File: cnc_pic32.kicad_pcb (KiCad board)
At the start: 4 copper layers, 96 x 96 mm, 121 parts, among them J1 icd, J10 tp_ft232_, J11 tp_ft232_, J12 tp_ft232_, J13 tp_ft232_, J14 tp_ft232_, J15 pololu, J16 pololu, J17 pololu, J18 pololu, J19 pololu, J2 USB_B_Mini, J20 pololu, J21 conector oled ST1306 128x32, J22 Adafruit ST7789, J23 mrf24j40_tp, J24 mrf24j40_tp, J3 tp_ft232_, J4 tp_ft232_, J5 USB_B_Mini, J6 tp_ft232_, J7 tp_ft232_, J8 tp_ft232_, J9 tp_ft232_, Q1 2N7002, SW1 power, SW2 up, SW3 down, SW4 left, SW5 rigth, U1 PIC32MX795F512L-80x-PF, U2 LM1117DT-3.3, U3 FT232BM, U4 LM1117DT-3.3, U5 MRF24J40MA, Y1 8MHZ, Y2 6MHZ

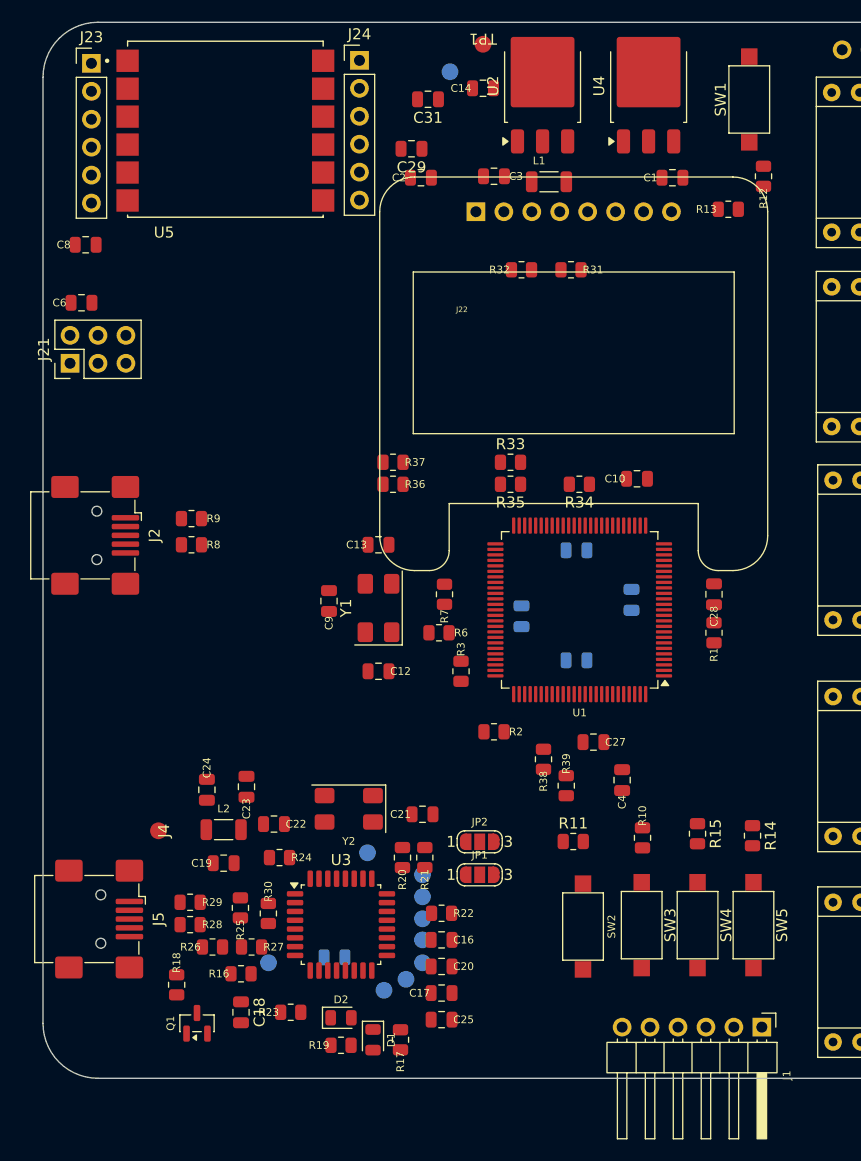
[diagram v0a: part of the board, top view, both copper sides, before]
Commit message: feat: 2-layer stackup, bus net class and schematic cleanup
PCB / project
- Reduce board from 4 layers to 2 (F.Cu / B.Cu) for cheaper fabrication
- Add "bus" net class and reorder net class priorities (bus 0, usb_differential 1, ...)

Schematics
- usb_conector_Ft232: add D+ / D-- labels on the USB mini-B data pair
- ft232: add 10K pull-ups, 100nf decoupling and test points on +3.3VA
- tp_ft232: remove solder jumpers JP1/JP2 (TX_Rpi / RX_Rpi now direct)
- Usb_pic32: add C38 100nf decoupling on +5V
- oled: expand connector J25 from 7 to 8 pins
- mcu / idc / power / zigbee / buttons / cnc_pic32: annotation and net cleanup

docs
- Add USB-Mini-B pinout reference images
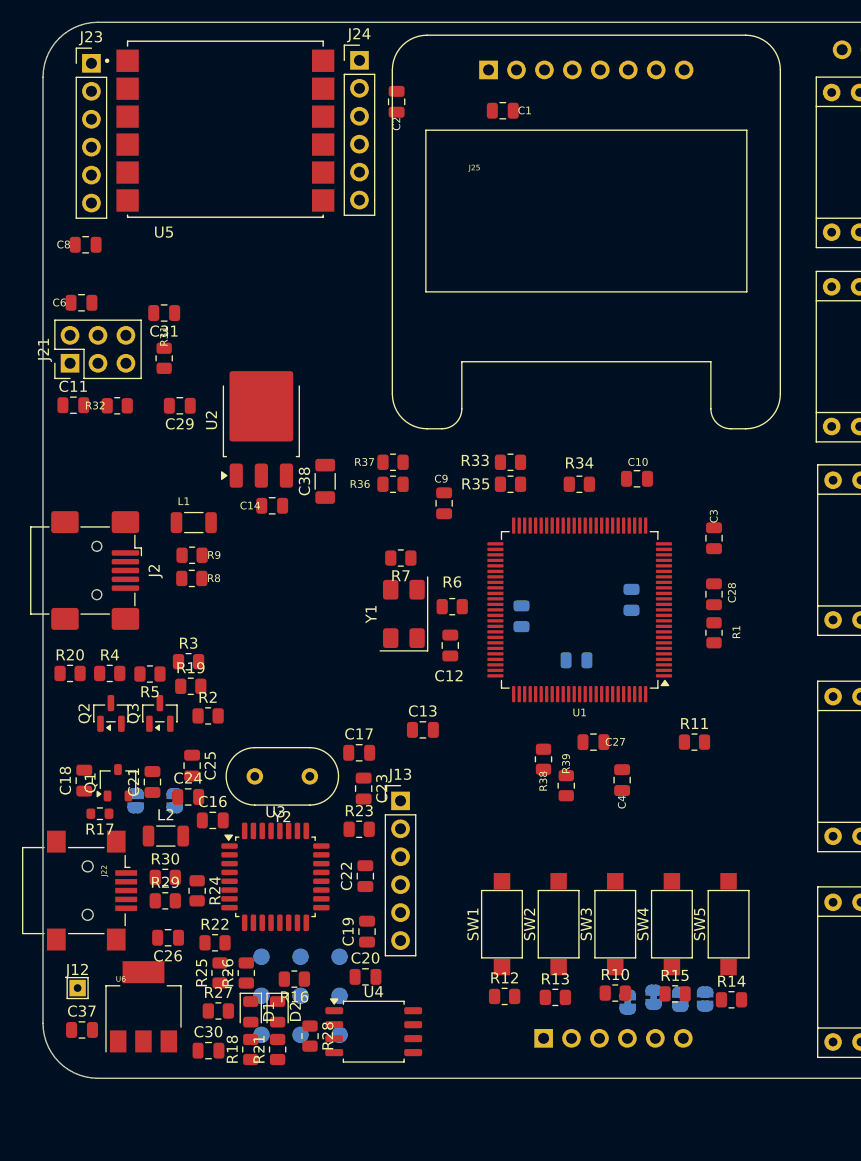
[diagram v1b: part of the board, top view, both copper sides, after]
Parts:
- removed J14: tp_ft232_, Library:connector_pin1
- removed TP1: tp_pic+5, Library:connector_pin1
- added C30: 100nf, Capacitor_SMD:C_0805_2012Metric, F.Cu at (67.0, 119.5)
- added C37: 100nf, Capacitor_SMD:C_0805_2012Metric, F.Cu at (55.5, 117.6)
- added C38: 100nf, Capacitor_SMD:C_1206_3216Metric, F.Cu at (77.7, 67.7)
- added J25: Conn_01x08_Pin, Library:Adafruit_SSD1306_No_Mounting_Holes_pads, F.Cu at (92.5, 30.3)
- added JP5: pgc1, Jumper:SolderJumper-2_P1.3mm_Open_RoundedPad1.0x1.5mm, B.Cu at (109.9, 114.8)
- added JP6: pgd1, Jumper:SolderJumper-2_P1.3mm_Open_RoundedPad1.0x1.5mm, B.Cu at (112.2, 114.8)
- added JP7: pgc2, Jumper:SolderJumper-2_P1.3mm_Bridged_RoundedPad1.0x1.5mm, B.Cu at (107.5, 114.6)
- added JP8: pgd2, Jumper:SolderJumper-2_P1.3mm_Bridged_RoundedPad1.0x1.5mm, B.Cu at (105.2, 115.1)
- added Q2: 2N7002, Package_TO_SOT_SMD:SOT-23, F.Cu at (58.2, 88.8)
- added Q3: 2N7002, Package_TO_SOT_SMD:SOT-23, F.Cu at (62.6, 88.8)
- added R4: 2k2, Resistor_SMD:R_0805_2012Metric, F.Cu at (58.1, 85.2)
- added R5: 2k2, Resistor_SMD:R_0805_2012Metric, F.Cu at (61.7, 85.2)
- added U6: LM1117DT-3.3, kiC:SOT-223-3_TabPin2, F.Cu at (61.1, 115.5)
- C11: moved to F.Cu
- C17, C18: value 33nf -> 100nf
- C21, C22: value 15p -> 100nf
- C23, C25: value 100nf -> 15p
- C24: value 100nf -> 33nf
- C26: value 100nf -> 33nf; moved to F.Cu
- J1: moved to B.Cu
- J10, J11, J3, J6, J7, J8, J9: value tp_ft232_ -> tp; footprint Library:connector_pin1 -> TestPoint:TestPoint_Pad_D1.5mm
- J12: value tp_ft232_ -> tp; footprint Library:connector_pin1 -> TestPoint:TestPoint_THTPad_1.5x1.5mm_Drill0.7mm; moved to F.Cu
- J13: value tp_ft232_ -> FT232RL; footprint Library:connector_pin1 -> Connector_PinHeader_2.54mm:PinHeader_1x06_P2.54mm_Vertical; moved to F.Cu
- J22: value Adafruit ST7789 -> USB_B_Mini; footprint Library:Adafruit_SSD1306_No_Mounting_Holes_pads -> kiC:USB_Mini-B_Lumberg_2486_01_Horizontal
- J4: value tp_ft232_ -> tp; footprint Library:connector_pin1 -> TestPoint:TestPoint_Pad_D1.5mm; moved to B.Cu
- J5: value USB_B_Mini -> tp; footprint Library:USB_Mini-B_Wuerth_65100516121_Horizontal -> TestPoint:TestPoint_Pad_D1.5mm; moved to B.Cu
- JP1, JP2: value SolderJumper_3_Bridged123 -> Jumper_Open; footprint Jumper:SolderJumper-3_P1.3mm_Open_RoundedPad1.0x1.5mm_NumberLabels -> Jumper:SolderJumper-2_P1.3mm_Open_RoundedPad1.0x1.5mm; moved to B.Cu
- Q1: value 2N7002 -> FDN306P; footprint Package_TO_SOT_SMD:SOT-23 -> Package_TO_SOT_SMD:SOT-23W
- R17: footprint Resistor_SMD:R_0805_2012Metric -> Resistor_SMD:R_0603_1608Metric
- R19: value 10K -> 100
- R2, R3: value 0 -> 2k2
- R21: value 100 -> 10K
- R23: value 10K -> 1K5
- R25: value 1K5 -> 10K
- R28: value 27 -> 2k2
- R30: value 10K -> 27
- U4: value LM1117DT-3.3 -> 93CxxA; footprint Package_TO_SOT_SMD:TO-252-3_TabPin2 -> Package_SO:SOIC-8_5.3x5.3mm_P1.27mm
- Y2: value 6MHZ -> Crystal; footprint Crystal:Crystal_SMD_0603-4Pin_6.0x3.5mm -> Crystal:Resonator-2Pin_W10.0mm_H5.0mm
- moved U4 89.5 mm to (82.1, 117.8), turned to 0 degrees
- moved SW1 78.3 mm to (93.7, 108.0)
- moved R12 78.2 mm to (94.0, 114.6), turned to 0 degrees
- moved R13 73.4 mm to (98.6, 114.6)
- moved J22 71.1 mm to (56.1, 104.9), turned to -90 degrees
- moved C11 47.6 mm to (54.8, 60.8)
- moved L1 44.7 mm to (65.7, 71.5)
- moved C14 42.5 mm to (72.8, 70.0)
- moved U2 39.7 mm to (71.9, 62.2)
- moved R32 38.8 mm to (58.7, 60.9)
- moved C3 38.5 mm to (113.0, 72.9), turned to -90 degrees
- moved R31 37.8 mm to (63.0, 56.5), turned to -90 degrees
- moved R19 35.4 mm to (65.4, 86.4)
- moved R20 34.5 mm to (54.5, 85.2), turned to 0 degrees
- moved R17 34.2 mm to (57.2, 97.9), turned to 180 degrees
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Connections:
- net /MCU/D+ renamed /D+
- net /MCU/D- renamed /D-
- net /MCU/RB0 renamed /MCU/PGC1
- net /MCU/RB1 renamed /MCU/PGD1
- net /MCU/RD4 renamed /RD4
- net /MCU/RD5 renamed /RD5
- net /MCU/RD6 renamed /RD6
- net /MCU/RF0 renamed /zigbee/MOSI_mrf
- net /MCU/RF1 renamed /zigbee/SCK_mrf
- net /MCU/RF12 renamed /zigbee/INT_mrf
- net /MCU/RF2 renamed /zigbee/MISO_mrf
- net /MCU/RF3 renamed /zigbee/CS_mrf
- net /MCU/RF4 renamed /zigbee/reset_mrf
- net /MCU/RF5 renamed /zigbee/wake_mrf
- net Net-(J2-D+) renamed /Usb_pic32/USB_D+
- net Net-(J2-D-) renamed /Usb_pic32/USB_D-
- A3 pad 16: /MCU/RB4 -> /MCU/PGM
- C14 pad 2: Net-(TP1-Pin_1) -> +5V
- C16 pad 1: /Ft232/mclr -> +3.3VA
- C16 pad 2: /Ft232/FT_CTS -> GND1
- C17 pad 1: Net-(U3-AVCC) -> +3.3VA
- C17 pad 2: GND -> GND1
- C18 pad 1: Net-(J3-Pin_1) -> Net-(C18-Pad1)
- C18 pad 2: GND -> +5VA
- C19 pad 1: GND -> GND1
- C19 pad 2: /Ft232/V+_USB -> +3.3VA
- C20 pad 1: GND -> GND1
- C20 pad 2: +3V3 -> +3.3VA
- C21 pad 1: /Ft232/FT_XTIN -> GND
- C21 pad 2: GND -> +5VA
- C22 pad 1: /Ft232/FT_XTOUT -> /Ft232/MCLR
- C22 pad 2: GND -> /Ft232/FT_CTS
- C23 pad 1: +3V3 -> /Ft232/FT_XTIN
- C24 pad 1: +3V3 -> Net-(U3-AVCC)
- C24 pad 2: GND -> GND1
- C25 pad 1: GND -> /Ft232/FT_XTOUT
- C25 pad 2: +3V3 -> GND
- C26 pad 1: GND -> Net-(J14-Pin_1)
- C26 pad 2: +3V3 -> GND1
- J1 pad 1: /Ft232/mclr -> /Ft232/MCLR
- J1 pad 4: /MCU/RC2 -> /Ft232/TX
- J1 pad 5: /MCU/RC3 -> /Ft232/RX
- J1 pad 6: /MCU/RC1 -> /MCU/PGM
- J12 pad 1: /Ft232/FT_RESET -> /Ft232/PWR
- J21 pad 1: GND -> +3.3V
- J21 pad 2: +3.3V -> +5V
- J21 pad 3: /MCU/sda -> /Oled/SDA
- J21 pad 4: /Oled/RG7 -> +5V
- J21 pad 5: /MCU/scl -> /Oled/SCL
- J21 pad 6: /Oled/RG8 -> GND
- J22 pad 1: GND -> Net-(J22-VBUS)
- J22 pad 2: +3.3V -> Net-(J22-D-)
- J22 pad 3: /MCU/sda -> Net-(J22-D+)
- J22 pad 4: /MCU/scl -> /Ft232/ID
- J22 pad 5: /Oled/RG0 -> GND
- J22 pad 6: /Oled/RG1 -> GND
- J3 pad 1: Net-(J3-Pin_1) -> /Ft232/FT_RST
- J4 pad 1: Net-(J4-Pin_1) -> /Ft232/FT_CTS
- J5 pad 1: Net-(J4-Pin_1) -> /Ft232/FT_DTR
- J6 pad 1: /Ft232/V+_USB -> /Ft232/FT_DRS
- J7 pad 1: /Ft232/FT_RI -> /Ft232/FT_DCD
- J8 pad 1: /Ft232/FT_DCD -> /Ft232/FT_RI
- J9 pad 1: /Ft232/FT_DRS -> /Ft232/FT
- JP1 pad 1: RXD -> /Ft232/TX
- JP1 pad 2: /Ft232/RX_MCU -> /Ft232/_TX
- JP2 pad 1: TXD -> /Ft232/RX
- JP2 pad 2: /Ft232/TX_MCU -> /Ft232/_RX
- L1 pad 2: Net-(TP1-Pin_1) -> +5V
- L2 pad 1: Net-(J4-Pin_1) -> Net-(J22-VBUS)
- L2 pad 2: /Ft232/V+_USB -> +5VA
- Q1 pad 1: Net-(Q1-G) -> Net-(C18-Pad1)
- Q1 pad 2: GND -> +5VA
- Q1 pad 3: Net-(Q1-D) -> /Ft232/PWR
- R1 pad 2: /Ft232/mclr -> /Ft232/MCLR
- R14 pad 2: /MCU/RD7 -> /RD7
- R16 pad 1: Net-(Q1-D) -> GND
- R16 pad 2: /Ft232/V+_USB -> /Ft232/FT_CTL
- R17 pad 1: GND -> Net-(C18-Pad1)
- R17 pad 2: /Ft232/FT -> /Ft232/FT_PWR_EN
- R18 pad 1: /Ft232/FT_PWR_EN -> +3.3VA
- R18 pad 2: Net-(Q1-G) -> Net-(D1-A)
- R19 pad 1: +3V3 -> Net-(U3-D0/TXD)
- R19 pad 2: Net-(D1-A) -> /Ft232/_TX
- R2 pad 1: /MCU/RD1 -> /Ft232/RX
- R2 pad 2: /MCU/sda -> +5VA
- R20 pad 1: Net-(U3-D0/TXD) -> Net-(U3-D1/RXD)
- R20 pad 2: /Ft232/RX_MCU -> /Ft232/_RX
- R21 pad 1: Net-(U3-D1/RXD) -> +3.3VA
- R21 pad 2: /Ft232/TX_MCU -> Net-(D2-A)
- R22 pad 1: +3V3 -> +3.3VA
- R22 pad 2: Net-(D2-A) -> Net-(U3-~{SLEEP})
- R23 pad 1: +3V3 -> Net-(U3-AVCC)
- R23 pad 2: Net-(U3-~{SLEEP}) -> +5VA
- R24 pad 1: Net-(U3-AVCC) -> /Ft232/FT_RST_OUT
- R24 pad 2: /Ft232/V+_USB -> /Ft232/FT_USB_DP
- R25 pad 1: /Ft232/FT_RST_OUT -> +3.3VA
- R25 pad 2: /Ft232/FT_USB_DP -> /Ft232/FT_RESET
- R27 pad 1: /Ft232/V+_USB -> +5VA
- R28 pad 1: /Ft232/FT_USB_BM -> /Ft232/FT_EEDATA
- R28 pad 2: Net-(J5-D+) -> Net-(U4-DO)
- R29 pad 2: Net-(J5-D-) -> Net-(J22-D+)
- R3 pad 1: /MCU/RD0 -> /Ft232/TX
- R3 pad 2: /MCU/scl -> +5VA
- R30 pad 1: +3V3 -> /Ft232/FT_USB_BM
- R30 pad 2: /Ft232/FT_RESET -> Net-(J22-D-)
- R31 pad 2: /MCU/scl -> /Oled/SCL
- R32 pad 2: /MCU/sda -> /Oled/SDA
- SW5 pad 1: /MCU/RD7 -> /RD7
- U1 pad 13: /Ft232/mclr -> /Ft232/MCLR
- U1 pad 21: /MCU/RB4 -> /MCU/PGM
- U1 pad 26: /Ft232/TX_MCU -> /Ft232/RX
- U1 pad 27: /Ft232/RX_MCU -> /Ft232/TX
- U2 pad 3: Net-(TP1-Pin_1) -> +5V
- U3 pad 13: +3V3 -> +3.3VA
- U3 pad 14: /Ft232/FT -> /Ft232/FT_CTL
- U3 pad 23: /Ft232/FT_RESET -> /Ft232/FT_RST
- U3 pad 26: /Ft232/V+_USB -> +5VA
- U3 pad 3: /Ft232/V+_USB -> +5VA
- U3 pad 6: Net-(J3-Pin_1) -> Net-(J14-Pin_1)
- U4 pad 1: GND -> /Ft232/FT_EECS
- U4 pad 2: +3V3 -> /Ft232/FT_EESK
- U4 pad 3: /Ft232/V+_USB -> /Ft232/FT_EEDATA
- Y2 pad 2: GND -> /Ft232/FT_XTOUT
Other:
- copper layers 4 -> 2
